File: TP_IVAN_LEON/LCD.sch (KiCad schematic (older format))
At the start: 4 parts, among them P2 CONN_02X08

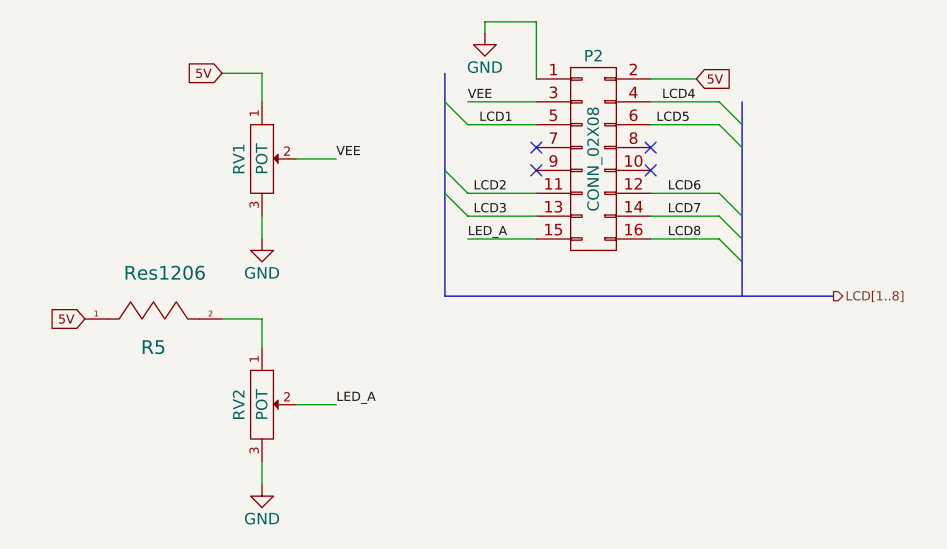
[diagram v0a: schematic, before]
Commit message: Agregado codigo digey key en 80% de componentes
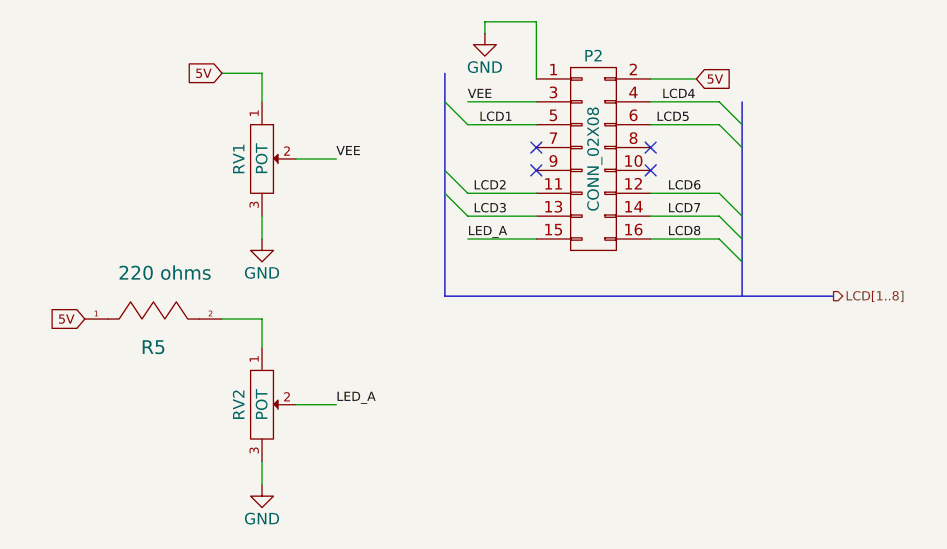
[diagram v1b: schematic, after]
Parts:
- P2: Digikey# (none) -> 952-2268-ND
- R5: value Res1206 -> 220 ohms; Digikey# (none) -> ERJ-T08J221V-ND
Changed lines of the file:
@@
 F 2 "TP:Pin_Header_Straight_2x08" H 5300 2125 50  0001 C CNN
 F 3 "" H 5300 2125 50  0000 C CNN
+F 4 "952-2268-ND" H 5300 3325 60  0001 C CNN "Digikey#"
 	1    5300 3325
 	1    0    0    -1
@@
 P 3350 4025
 F 0 "R5" H 3375 3900 60  0000 C CNN
-F 1 "Res1206" H 3425 4225 60  0000 C CNN
+F 1 "220 ohms" H 3425 4225 60  0000 C CNN
 F 2 "TP:Resistor_SMD+THTuniversal_1206_RM10_HandSoldering" H 3350 4025 60  0001 C CNN
 F 3 "" H 3350 4025 60  0000 C CNN
+F 4 "ERJ-T08J221V-ND" H 3350 4025 60  0001 C CNN "Digikey#"
 	1    3350 4025
 	1    0    0    -1

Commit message: Agregado cambios subrayados en verde descritos en documento Leonv.ods en la carpeta docs
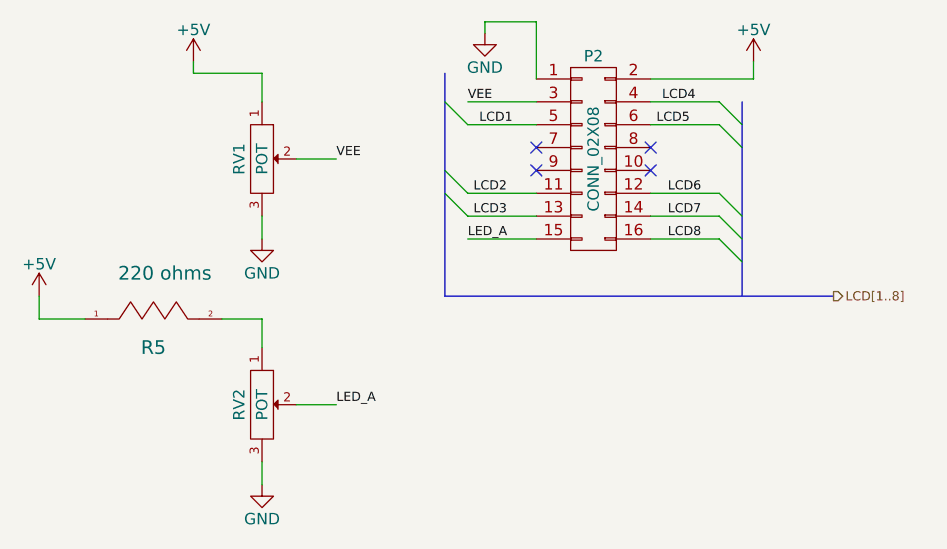
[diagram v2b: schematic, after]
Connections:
- net 5V renamed +5V
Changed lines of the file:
@@
 $Descr A4 11693 8268
 encoding utf-8
-Sheet 5 6
+Sheet 3 4
 Title "Conexión del LCD alfanumerico"
 Date "12/07/2016"
@@
 $EndComp
 $Comp
-L GND #PWR08
+L GND #PWR05
 U 1 1 57993A55
 P 4825 2775
-F 0 "#PWR08" H 4825 2525 50  0001 C CNN
+F 0 "#PWR05" H 4825 2525 50  0001 C CNN
 F 1 "GND" H 4825 2625 50  0000 C CNN
 F 2 "" H 4825 2775 50  0000 C CNN
@@
 	1    0    0    -1
 $EndComp
-Text GLabel 5750 2975 2    40   Input ~ 0
-5V
-Wire Wire Line
-	5750 2975 5550 2975
+Wire Wire Line
+	5550 2975 6000 2975
 Wire Bus Line
 	5950 3075 5950 3925
@@
 Wire Wire Line
 	4000 3325 4175 3325
-Text GLabel 3675 2950 0    40   Input ~ 0
-5V
-$Comp
-L GND #PWR09
+$Comp
+L GND #PWR06
 U 1 1 57993FAF
 P 3850 3675
-F 0 "#PWR09" H 3850 3425 50  0001 C CNN
+F 0 "#PWR06" H 3850 3425 50  0001 C CNN
 F 1 "GND" H 3850 3525 50  0000 C CNN
 F 2 "" H 3850 3675 50  0000 C CNN
@@
 $EndComp
 Wire Wire Line
-	3675 2950 3850 2950
+	3550 2950 3850 2950
 Wire Wire Line
 	3850 2950 3850 3075
@@
 Wire Wire Line
 	4000 4400 4175 4400
-Text GLabel 3075 4025 0    40   Input ~ 0
-5V
-$Comp
-L GND #PWR010
+$Comp
+L GND #PWR07
 U 1 1 57994190
 P 3850 4750
-F 0 "#PWR010" H 3850 4500 50  0001 C CNN
+F 0 "#PWR07" H 3850 4500 50  0001 C CNN
 F 1 "GND" H 3850 4600 50  0000 C CNN
 F 2 "" H 3850 4750 50  0000 C CNN
@@
 Text Label 5625 3675 0    40   ~ 0
 LCD8
+$Comp
+L +5V #PWR08
+U 1 1 57B98EA6
+P 3550 2900
+F 0 "#PWR08" H 3550 2750 50  0001 C CNN
+F 1 "+5V" H 3550 3040 50  0000 C CNN
+F 2 "" H 3550 2900 50  0000 C CNN
+F 3 "" H 3550 2900 50  0000 C CNN
+	1    3550 2900
+	1    0    0    -1
+$EndComp
+$Comp
+L +5V #PWR09
+U 1 1 57B98EFE
+P 2875 3925
+F 0 "#PWR09" H 2875 3775 50  0001 C CNN
+F 1 "+5V" H 2875 4065 50  0000 C CNN
+F 2 "" H 2875 3925 50  0000 C CNN
+F 3 "" H 2875 3925 50  0000 C CNN
+	1    2875 3925
+	1    0    0    -1
+$EndComp
+$Comp
+L +5V #PWR010
+U 1 1 57B98FAE
+P 6000 2900
+F 0 "#PWR010" H 6000 2750 50  0001 C CNN
+F 1 "+5V" H 6000 3040 50  0000 C CNN
+F 2 "" H 6000 2900 50  0000 C CNN
+F 3 "" H 6000 2900 50  0000 C CNN
+	1    6000 2900
+	1    0    0    -1
+$EndComp
+Wire Wire Line
+	3075 4025 2875 4025
+Wire Wire Line
+	2875 4025 2875 3925
+Wire Wire Line
+	3550 2950 3550 2900
+Wire Wire Line
+	6000 2975 6000 2900
 $EndSCHEMATC

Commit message: Agrego Manf y Manf# en todos los componentes
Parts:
- P2: Manf (none) -> M20-9990546; Manf# (none) -> Harwin Inc.
- R5: Manf (none) -> Panasonic Electronic Components; Manf# (none) -> ERJ-T08J221V
- RV1, RV2: Digikey# (none) -> WM1732-ND; Manf (none) -> Molex, LLC; Manf# (none) -> 0530470310
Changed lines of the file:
@@
 F 3 "" H 5300 2125 50  0000 C CNN
 F 4 "952-2268-ND" H 5300 3325 60  0001 C CNN "Digikey#"
+F 5 "Harwin Inc." H 5300 3325 60  0001 C CNN "Manf#"
+F 6 "M20-9990546" H 5300 3325 60  0001 C CNN "Manf"
 	1    5300 3325
 	1    0    0    -1
@@
 F 2 "TP:Connector_Molex_PicoBlade_53047-0310" H 3850 3325 50  0001 C CNN
 F 3 "" H 3850 3325 50  0000 C CNN
+F 4 "WM1732-ND" H 3850 3325 60  0001 C CNN "Digikey#"
+F 5 "0530470310" H 3850 3325 60  0001 C CNN "Manf#"
+F 6 "Molex, LLC" H 3850 3325 60  0001 C CNN "Manf"
 	1    3850 3325
 	0    1    1    0
@@
 Text Label 4175 3325 0    40   ~ 0
 VEE
-$Comp
-L POT RV2
-U 1 1 57994188
-P 3850 4400
-F 0 "RV2" H 3850 4300 50  0000 C CNN
-F 1 "POT" H 3850 4400 50  0000 C CNN
-F 2 "TP:Connector_Molex_PicoBlade_53047-0310" H 3850 4400 50  0001 C CNN
-F 3 "" H 3850 4400 50  0000 C CNN
-	1    3850 4400
-	0    1    1    0
-$EndComp
 Wire Wire Line
 	4000 4400 4175 4400
@@
 F 3 "" H 3350 4025 60  0000 C CNN
 F 4 "ERJ-T08J221V-ND" H 3350 4025 60  0001 C CNN "Digikey#"
+F 5 "ERJ-T08J221V" H 3350 4025 60  0001 C CNN "Manf#"
+F 6 "Panasonic Electronic Components" H 3350 4025 60  0001 C CNN "Manf"
 	1    3350 4025
 	1    0    0    -1
@@
 Wire Wire Line
 	6000 2975 6000 2900
+$Comp
+L POT RV2
+U 1 1 57BFC77A
+P 3850 4400
+F 0 "RV2" H 3850 4300 50  0000 C CNN
+F 1 "POT" H 3850 4400 50  0000 C CNN
+F 2 "TP:Connector_Molex_PicoBlade_53047-0310" H 3850 4400 50  0001 C CNN
+F 3 "" H 3850 4400 50  0000 C CNN
+F 4 "WM1732-ND" H 3850 4400 60  0001 C CNN "Digikey#"
+F 5 "0530470310" H 3850 4400 60  0001 C CNN "Manf#"
+F 6 "Molex, LLC" H 3850 4400 60  0001 C CNN "Manf"
+	1    3850 4400
+	0    1    1    0
+$EndComp
 $EndSCHEMATC
